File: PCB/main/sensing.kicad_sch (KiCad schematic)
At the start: 4 parts

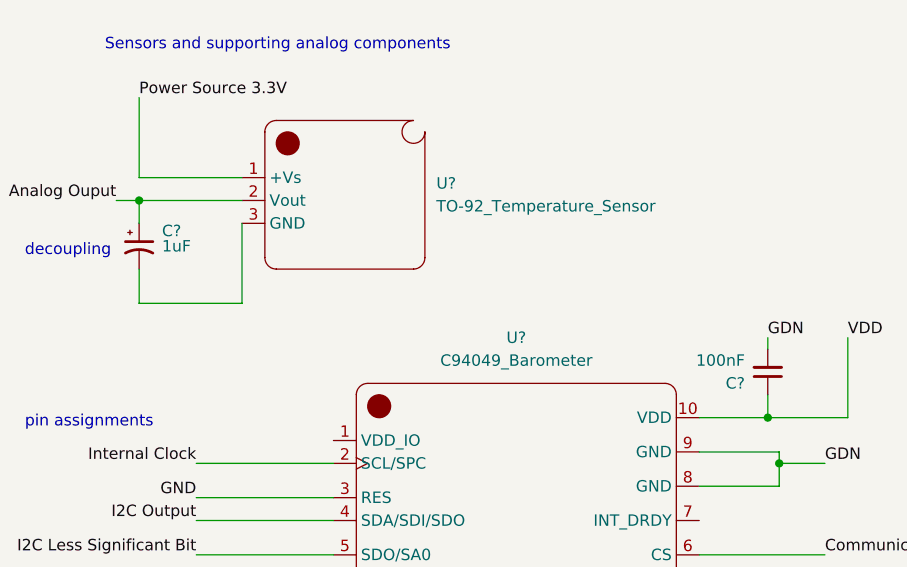
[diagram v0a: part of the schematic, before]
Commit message: Finished v0.1 of MC Interfacing schem
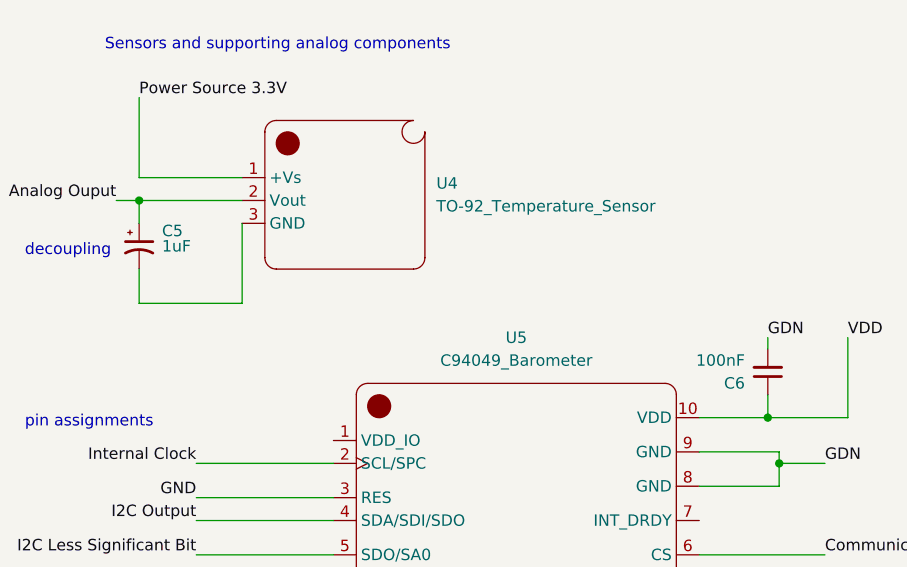
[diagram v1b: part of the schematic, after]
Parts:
- gave numbers to parts that had none: 4
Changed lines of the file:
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@@
   (symbol (lib_id "AAA 3088F:TO-92_Temperature_Sensor") (at 57.15 33.02 0) (unit 1)
     (in_bom yes) (on_board yes) (fields_autoplaced)
-    (property "Reference" "U?" (id 0) (at 67.31 31.1149 0)
+    (property "Reference" "U4" (id 0) (at 67.31 31.1149 0)
       (effects (font (size 1.27 1.27)) (justify left))
     )
@@
   (symbol (lib_id "AAA 3088F:_C94049_Barometer") (at 76.2 67.31 0) (unit 1)
     (in_bom yes) (on_board yes) (fields_autoplaced)
-    (property "Reference" "U?" (id 0) (at 76.2 48.26 0))
+    (property "Reference" "U5" (id 0) (at 76.2 48.26 0))
     (property "Value" "C94049_Barometer" (id 1) (at 76.2 50.8 0))
     (property "Footprint" "" (id 2) (at 76.2 67.31 0)
@@
   (symbol (lib_id "Device:C_Polarized_Small_US") (at 34.29 38.1 0) (unit 1)
     (in_bom yes) (on_board yes)
-    (property "Reference" "C?" (id 0) (at 36.83 36.3981 0)
+    (property "Reference" "C5" (id 0) (at 36.83 36.3981 0)
       (effects (font (size 1.27 1.27)) (justify left))
     )
@@
   (symbol (lib_id "Device:C_Small") (at 104.14 52.07 180) (unit 1)
     (in_bom yes) (on_board yes) (fields_autoplaced)
-    (property "Reference" "C?" (id 0) (at 101.6 53.3338 0)
+    (property "Reference" "C6" (id 0) (at 101.6 53.3338 0)
       (effects (font (size 1.27 1.27)) (justify left))
     )

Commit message: Finished initial design
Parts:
- U4: value TO-92_Temperature_Sensor -> LM61BIZ/NOPD_TempSensor(TO-92)
- U5: value C94049_Barometer -> LPS22HBTR_Barometer
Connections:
- net Communication Pin (set 1) is gone; now on net COMM: U5.6 (CS)
- net GDN is gone; now on net GND: C6.2, U5.8 (GND), U5.9 (GND)
- net GND: now also C5.2, U4.3 (GND)
- net COMM: now reaches U5.1 (VDD_IO)
- net Analog Ouput renamed TEMP_OUT
- net I2C Less Significant Bit renamed BARO_LSB
- net I2C Output renamed BARO_SDA
- net Internal Clock renamed BARO_SCL
- net Power Source 3.3V renamed TEMP_VCC
- net VDD renamed BARO_VDD
- no-connect marks 0 -> 1
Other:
- note added: "ANALOG SENSOR"
- note added: "Analog Sensor and supporting analog components"
- note added: "DIGITAL SENSOR"
- note added: "Digital Sensor and supporting analog components"
- note removed: "Sensors and supporting analog components"
- company: (none) -> University of Cape Town
- title: (none) -> Sensing Subsystem
- moved on the sheet: C5, C6, U4, U5

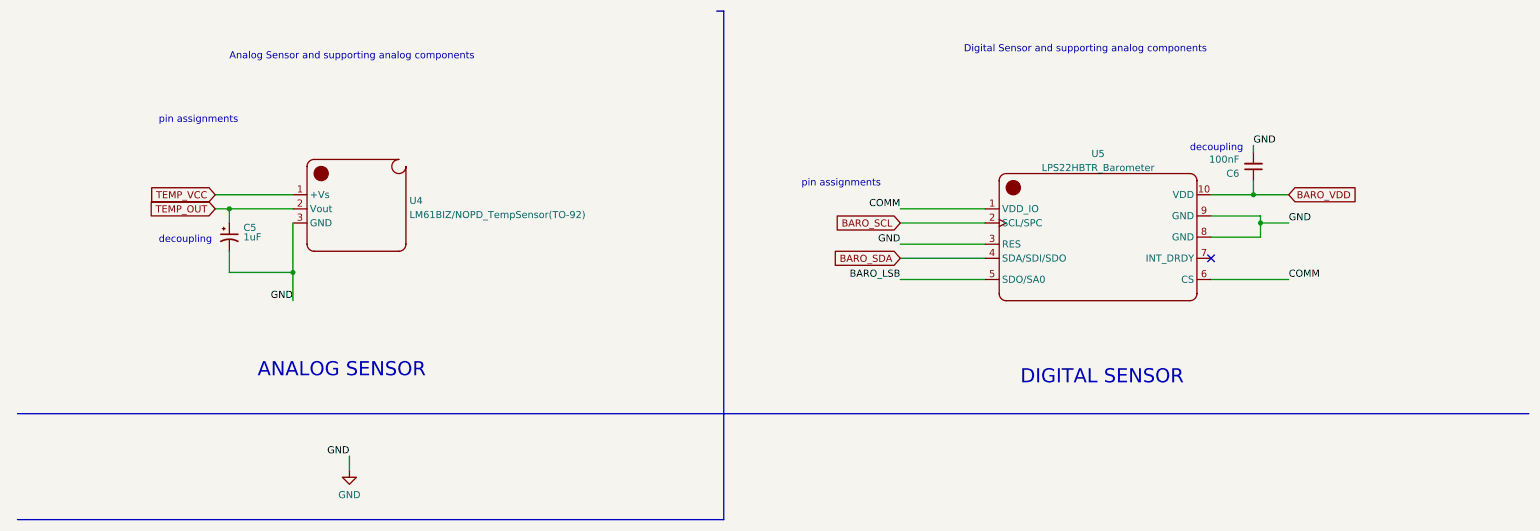
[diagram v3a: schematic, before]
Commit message: Fiddled a bit with labels
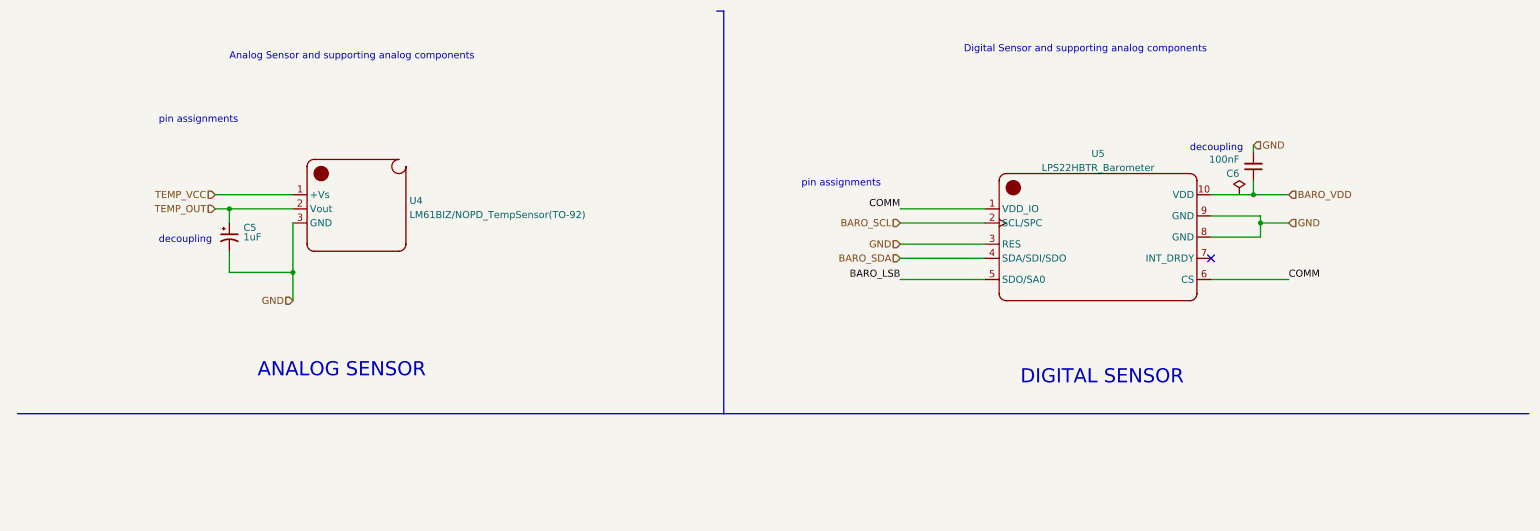
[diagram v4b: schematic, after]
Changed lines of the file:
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@@
-    (stroke (width 0) (type default) (color 0 0 0 0))
-  )
-  (wire (pts (xy 72.39 91.44) (xy 72.39 93.98))
     (stroke (width 0) (type default) (color 0 0 0 0))
   )
@@
     (stroke (width 0) (type default) (color 0 0 0 0))
   )
-  (polyline (pts (xy 139.7 102.87) (xy 12.7 102.87))
-    (stroke (width 0) (type default) (color 0 0 0 0))
-  )
   (wire (pts (xy 234.95 35.56) (xy 234.95 36.83))
-    (stroke (width 0) (type default) (color 0 0 0 0))
-  )
-  (polyline (pts (xy 139.7 83.82) (xy 139.7 102.87))
     (stroke (width 0) (type default) (color 0 0 0 0))
   )
@@
     (effects (font (size 1.27 1.27)) (justify left bottom))
   )
-  (label "GND" (at 234.95 35.56 0)
-    (effects (font (size 1.27 1.27)) (justify left bottom))
-  )
-  (label "GND" (at 171.45 53.34 180)
-    (effects (font (size 1.27 1.27)) (justify right bottom))
-  )
   (label "COMM" (at 171.45 46.99 180)
     (effects (font (size 1.27 1.27)) (justify right bottom))
-  )
-  (label "GND" (at 241.3 49.53 0)
-    (effects (font (size 1.27 1.27)) (justify left bottom))
   )
   (label "COMM" (at 241.3 59.69 0)
@@
     (effects (font (size 1.27 1.27)) (justify right bottom))
   )
-  (label "GND" (at 62.23 63.5 180)
-    (effects (font (size 1.27 1.27)) (justify right bottom))
+  (hierarchical_label "TEMP_OUT" (shape input) (at 48.26 46.99 180)
+    (effects (font (size 1.27 1.27)) (justify right))
   )
-  (label "GND" (at 72.39 91.44 180)
-    (effects (font (size 1.27 1.27)) (justify right bottom))
+  (hierarchical_label "GND" (shape input) (at 171.45 53.34 180)
+    (effects (font (size 1.27 1.27)) (justify right))
   )
-  (global_label "BARO_SCL" (shape input) (at 171.45 49.53 180) (fields_autoplaced)
+  (hierarchical_label "GND" (shape input) (at 62.23 63.5 180)
     (effects (font (size 1.27 1.27)) (justify right))
-    (property "Intersheet References" "${INTERSHEET_REFS}" (id 0) (at 159.6026 49.4506 0)
-      (effects (font (size 1.27 1.27)) (justify right) hide)
-    )
   )
-  (global_label "TEMP_VCC" (shape input) (at 48.26 44.45 180) (fields_autoplaced)
+  (hierarchical_label "GND" (shape input) (at 241.3 49.53 0)
+    (effects (font (size 1.27 1.27)) (justify left))
+  )
+  (hierarchical_label "BARO_SDA" (shape input) (at 171.45 55.88 180)
     (effects (font (size 1.27 1.27)) (justify right))
-    (property "Intersheet References" "${INTERSHEET_REFS}" (id 0) (at 36.4126 44.5294 0)
-      (effects (font (size 1.27 1.27)) (justify right) hide)
-    )
   )
-  (global_label "TEMP_OUT" (shape input) (at 48.26 46.99 180) (fields_autoplaced)
+  (hierarchical_label "GND" (shape input) (at 234.95 35.56 0)
+    (effects (font (size 1.27 1.27)) (justify left))
+  )
+  (hierarchical_label "BARO_VDD" (shape input) (at 241.3 44.45 0)
+    (effects (font (size 1.27 1.27)) (justify left))
+  )
+  (hierarchical_label "TEMP_VCC" (shape input) (at 48.26 44.45 180)
     (effects (font (size 1.27 1.27)) (justify right))
-    (property "Intersheet References" "${INTERSHEET_REFS}" (id 0) (at 36.4126 46.9106 0)
-      (effects (font (size 1.27 1.27)) (justify right) hide)
-    )
   )
-  (global_label "BARO_SDA" (shape input) (at 171.45 55.88 180) (fields_autoplaced)
+  (hierarchical_label "BARO_SCL" (shape input) (at 171.45 49.53 180)
     (effects (font (size 1.27 1.27)) (justify right))
-    (property "Intersheet References" "${INTERSHEET_REFS}" (id 0) (at 159.5421 55.8006 0)
-      (effects (font (size 1.27 1.27)) (justify right) hide)
-    )
   )
-  (global_label "BARO_VDD" (shape input) (at 241.3 44.45 0) (fields_autoplaced)
-    (effects (font (size 1.27 1.27)) (justify left))
-    (property "Intersheet References" "${INTERSHEET_REFS}" (id 0) (at 253.2683 44.3706 0)
-      (effects (font (size 1.27 1.27)) (justify left) hide)
-    )
-  )
-  (symbol (lib_id "power:GND") (at 72.39 93.98 0) (unit 1)
+  (symbol (lib_id "power:PWR_FLAG") (at 232.41 44.45 0) (unit 1)
     (in_bom yes) (on_board yes) (fields_autoplaced)
-    (property "Reference" "#PWR019" (id 0) (at 72.39 100.33 0)
+    (property "Reference" "#FLG01" (id 0) (at 232.41 42.545 0)
       (effects (font (size 1.27 1.27)) hide)
     )
-    (property "Value" "GND" (id 1) (at 72.39 98.4234 0))
-    (property "Footprint" "" (id 2) (at 72.39 93.98 0)
+    (property "Value" "PWR_FLAG" (id 1) (at 232.41 40.8742 0)
       (effects (font (size 1.27 1.27)) hide)
     )
-    (property "Datasheet" "" (id 3) (at 72.39 93.98 0)
+    (property "Footprint" "" (id 2) (at 232.41 44.45 0)
       (effects (font (size 1.27 1.27)) hide)
     )
+    (property "Datasheet" "~" (id 3) (at 232.41 44.45 0)
+      (effects (font (size 1.27 1.27)) hide)
+    )

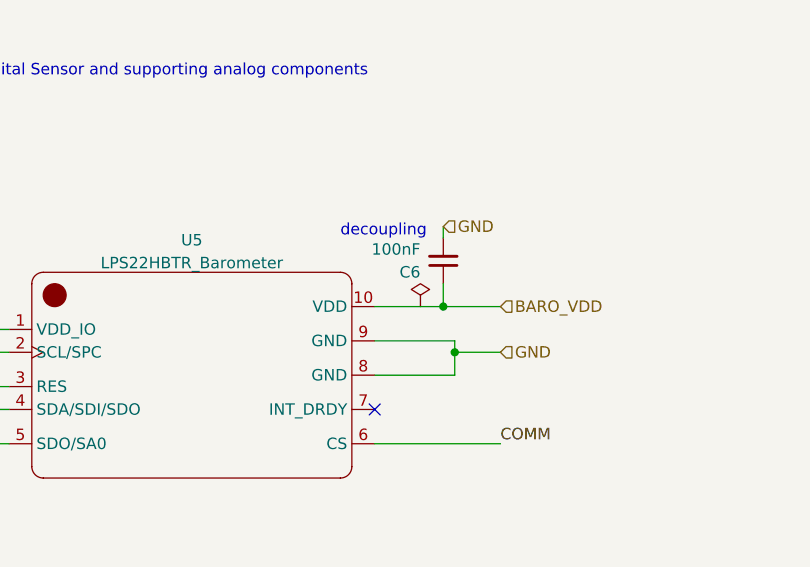
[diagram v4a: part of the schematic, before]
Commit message: Added Footprint and symbol files
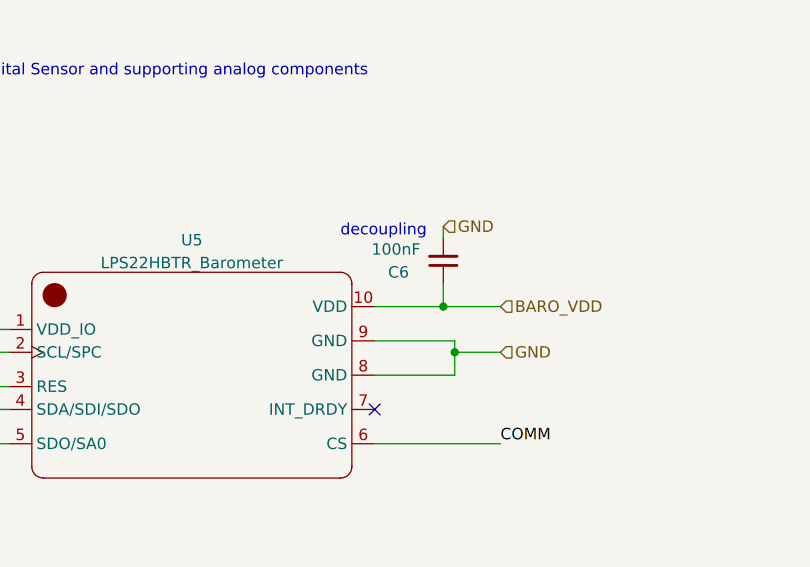
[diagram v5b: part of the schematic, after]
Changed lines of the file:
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@@
+    (stroke (width 0) (type default) (color 0 0 0 0))
+  )
+  (wire (pts (xy 171.45 46.99) (xy 186.69 46.99))
+    (stroke (width 0) (type default) (color 0 0 0 0))
+  )
+  (wire (pts (xy 48.26 46.99) (xy 50.8 46.99))
+    (stroke (width 0) (type default) (color 0 0 0 0))
+  )
+  (wire (pts (xy 171.45 55.88) (xy 186.69 55.88))
+    (stroke (width 0) (type default) (color 0 0 0 0))
+  )
+  (wire (pts (xy 171.45 49.53) (xy 186.69 49.53))
+    (stroke (width 0) (type default) (color 0 0 0 0))
+  )
+  (polyline (pts (xy 12.7 83.82) (xy 139.7 83.82))
+    (stroke (width 0) (type default) (color 0 0 0 0))
+  )
+  (wire (pts (xy 62.23 63.5) (xy 62.23 58.42))
+    (stroke (width 0) (type default) (color 0 0 0 0))
+  )
+  (wire (pts (xy 171.45 59.69) (xy 186.69 59.69))
+    (stroke (width 0) (type default) (color 0 0 0 0))
+  )
+  (wire (pts (xy 62.23 49.53) (xy 62.23 58.42))
+    (stroke (width 0) (type default) (color 0 0 0 0))
+  )
+  (wire (pts (xy 227.33 59.69) (xy 241.3 59.69))
+    (stroke (width 0) (type default) (color 0 0 0 0))
+  )
+  (wire (pts (xy 50.8 46.99) (xy 50.8 49.53))
+    (stroke (width 0) (type default) (color 0 0 0 0))
+  )
+  (polyline (pts (xy 139.7 83.82) (xy 284.48 83.82))
+    (stroke (width 0) (type default) (color 0 0 0 0))
+  )
+  (wire (pts (xy 234.95 44.45) (xy 241.3 44.45))
+    (stroke (width 0) (type default) (color 0 0 0 0))
+  )
+  (wire (pts (xy 234.95 35.56) (xy 234.95 36.83))
+    (stroke (width 0) (type default) (color 0 0 0 0))
+  )
+  (polyline (pts (xy 139.7 83.82) (xy 139.7 11.43))
+    (stroke (width 0) (type default) (color 0 0 0 0))
+  )
+  (wire (pts (xy 227.33 48.26) (xy 236.22 48.26))
+    (stroke (width 0) (type default) (color 0 0 0 0))
+  )
+  (wire (pts (xy 236.22 49.53) (xy 241.3 49.53))
+    (stroke (width 0) (type default) (color 0 0 0 0))
+  )
+  (wire (pts (xy 236.22 48.26) (xy 236.22 49.53))
+    (stroke (width 0) (type default) (color 0 0 0 0))
+  )
+  (wire (pts (xy 48.26 44.45) (xy 62.23 44.45))
+    (stroke (width 0) (type default) (color 0 0 0 0))
+  )
+  (wire (pts (xy 171.45 53.34) (xy 186.69 53.34))
+    (stroke (width 0) (type default) (color 0 0 0 0))
+  )
+  (wire (pts (xy 62.23 58.42) (xy 50.8 58.42))
+    (stroke (width 0) (type default) (color 0 0 0 0))
+  )
+  (wire (pts (xy 50.8 54.61) (xy 50.8 58.42))
+    (stroke (width 0) (type default) (color 0 0 0 0))
+  )
+  (wire (pts (xy 227.33 52.07) (xy 236.22 52.07))
+    (stroke (width 0) (type default) (color 0 0 0 0))
+  )
+  (polyline (pts (xy 139.7 11.43) (xy 138.43 11.43))
+    (stroke (width 0) (type default) (color 0 0 0 0))
+  )
+  (wire (pts (xy 236.22 49.53) (xy 236.22 52.07))
     (stroke (width 0) (type default) (color 0 0 0 0))
   )
   (wire (pts (xy 227.33 44.45) (xy 234.95 44.45))
-    (stroke (width 0) (type default) (color 0 0 0 0))
-  )
-  (wire (pts (xy 171.45 46.99) (xy 186.69 46.99))
-    (stroke (width 0) (type default) (color 0 0 0 0))
-  )
-  (wire (pts (xy 48.26 46.99) (xy 50.8 46.99))
-    (stroke (width 0) (type default) (color 0 0 0 0))
-  )
-  (wire (pts (xy 171.45 55.88) (xy 186.69 55.88))
-    (stroke (width 0) (type default) (color 0 0 0 0))
-  )
-  (wire (pts (xy 171.45 49.53) (xy 186.69 49.53))
-    (stroke (width 0) (type default) (color 0 0 0 0))
-  )
-  (polyline (pts (xy 12.7 83.82) (xy 139.7 83.82))
-    (stroke (width 0) (type default) (color 0 0 0 0))
-  )
-  (wire (pts (xy 62.23 63.5) (xy 62.23 58.42))
-    (stroke (width 0) (type default) (color 0 0 0 0))
-  )
-  (wire (pts (xy 171.45 59.69) (xy 186.69 59.69))
-    (stroke (width 0) (type default) (color 0 0 0 0))
-  )
-  (wire (pts (xy 62.23 49.53) (xy 62.23 58.42))
-    (stroke (width 0) (type default) (color 0 0 0 0))
-  )
-  (wire (pts (xy 227.33 59.69) (xy 241.3 59.69))
-    (stroke (width 0) (type default) (color 0 0 0 0))
-  )
-  (wire (pts (xy 50.8 46.99) (xy 50.8 49.53))
-    (stroke (width 0) (type default) (color 0 0 0 0))
-  )
-  (polyline (pts (xy 139.7 83.82) (xy 284.48 83.82))
-    (stroke (width 0) (type default) (color 0 0 0 0))
-  )
-  (wire (pts (xy 234.95 44.45) (xy 241.3 44.45))
-    (stroke (width 0) (type default) (color 0 0 0 0))
-  )
-  (wire (pts (xy 234.95 35.56) (xy 234.95 36.83))
-    (stroke (width 0) (type default) (color 0 0 0 0))
-  )
-  (polyline (pts (xy 139.7 83.82) (xy 139.7 11.43))
-    (stroke (width 0) (type default) (color 0 0 0 0))
-  )
-  (wire (pts (xy 227.33 48.26) (xy 236.22 48.26))
-    (stroke (width 0) (type default) (color 0 0 0 0))
-  )
-  (wire (pts (xy 236.22 49.53) (xy 241.3 49.53))
-    (stroke (width 0) (type default) (color 0 0 0 0))
-  )
-  (wire (pts (xy 236.22 48.26) (xy 236.22 49.53))
-    (stroke (width 0) (type default) (color 0 0 0 0))
-  )
-  (wire (pts (xy 48.26 44.45) (xy 62.23 44.45))
-    (stroke (width 0) (type default) (color 0 0 0 0))
-  )
-  (wire (pts (xy 171.45 53.34) (xy 186.69 53.34))
-    (stroke (width 0) (type default) (color 0 0 0 0))
-  )
-  (wire (pts (xy 62.23 58.42) (xy 50.8 58.42))
-    (stroke (width 0) (type default) (color 0 0 0 0))
-  )
-  (wire (pts (xy 50.8 54.61) (xy 50.8 58.42))
-    (stroke (width 0) (type default) (color 0 0 0 0))
-  )
-  (wire (pts (xy 227.33 52.07) (xy 236.22 52.07))
-    (stroke (width 0) (type default) (color 0 0 0 0))
-  )
-  (polyline (pts (xy 139.7 11.43) (xy 138.43 11.43))
-    (stroke (width 0) (type default) (color 0 0 0 0))
-  )
-  (wire (pts (xy 236.22 49.53) (xy 236.22 52.07))
     (stroke (width 0) (type default) (color 0 0 0 0))
   )
@@
   (hierarchical_label "BARO_SCL" (shape input) (at 171.45 49.53 180)
     (effects (font (size 1.27 1.27)) (justify right))
-  )
-  (symbol (lib_id "power:PWR_FLAG") (at 232.41 44.45 0) (unit 1)
-    (in_bom yes) (on_board yes) (fields_autoplaced)
-    (property "Reference" "#FLG01" (id 0) (at 232.41 42.545 0)
-      (effects (font (size 1.27 1.27)) hide)
-    )
-    (property "Value" "PWR_FLAG" (id 1) (at 232.41 40.8742 0)
-      (effects (font (size 1.27 1.27)) hide)
-    )
-    (property "Footprint" "" (id 2) (at 232.41 44.45 0)
-      (effects (font (size 1.27 1.27)) hide)
-    )
-    (property "Datasheet" "~" (id 3) (at 232.41 44.45 0)
-      (effects (font (size 1.27 1.27)) hide)
-    )
-    (pin "1")
   )
   (symbol (lib_id "AAA 3088F:TO-92_Temperature_Sensor") (at 73.66 46.99 0) (unit 1)
@@
   )
   (symbol (lib_id "Device:C_Small") (at 234.95 39.37 180) (unit 1)
-    (in_bom yes) (on_board yes) (fields_autoplaced)
-    (property "Reference" "C6" (id 0) (at 232.41 40.6338 0)
-      (effects (font (size 1.27 1.27)) (justify left))
-    )
+    (in_bom yes) (on_board yes)
+    (property "Reference" "C6" (id 0) (at 231.14 40.64 0)
+      (effects (font (size 1.27 1.27)) (justify left))
+    )
